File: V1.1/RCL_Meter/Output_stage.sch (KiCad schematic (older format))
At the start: 19 parts

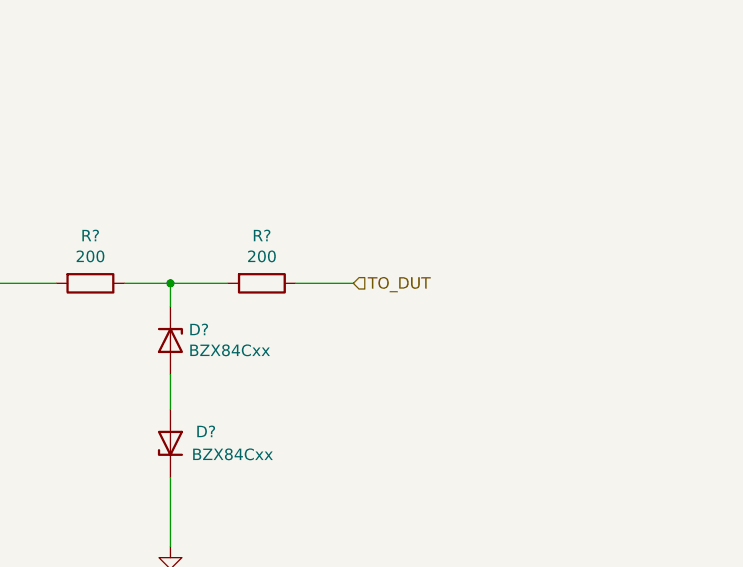
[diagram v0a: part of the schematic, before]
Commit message: Added voltage and current front end
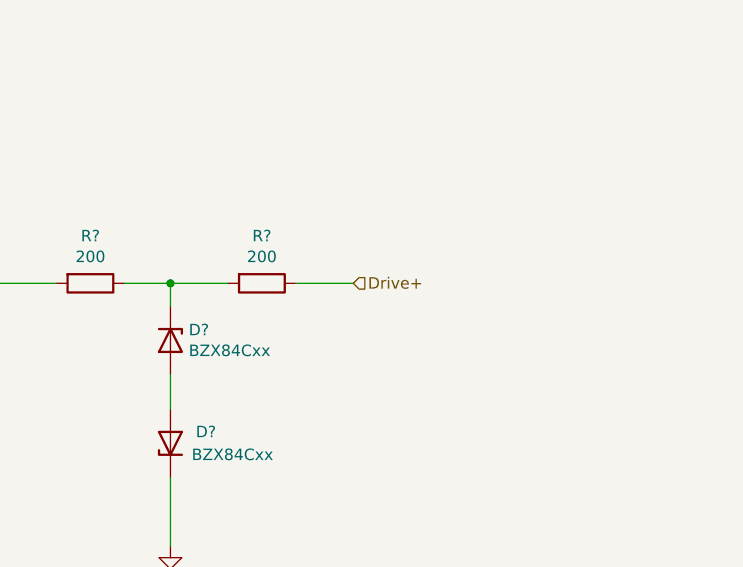
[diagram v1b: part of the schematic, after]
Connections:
- net TO_DUT renamed Drive+
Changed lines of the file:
@@
 $Descr A4 11693 8268
 encoding utf-8
-Sheet 2 2
+Sheet 2 3
 Title ""
 Date ""
@@
 	3950 4950 3700 4950
 Text HLabel 8200 4750 2    50   Input ~ 0
-TO_DUT
+Drive+
 Wire Wire Line
 	8200 4750 7950 4750
